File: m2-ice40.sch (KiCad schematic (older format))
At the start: 0 parts

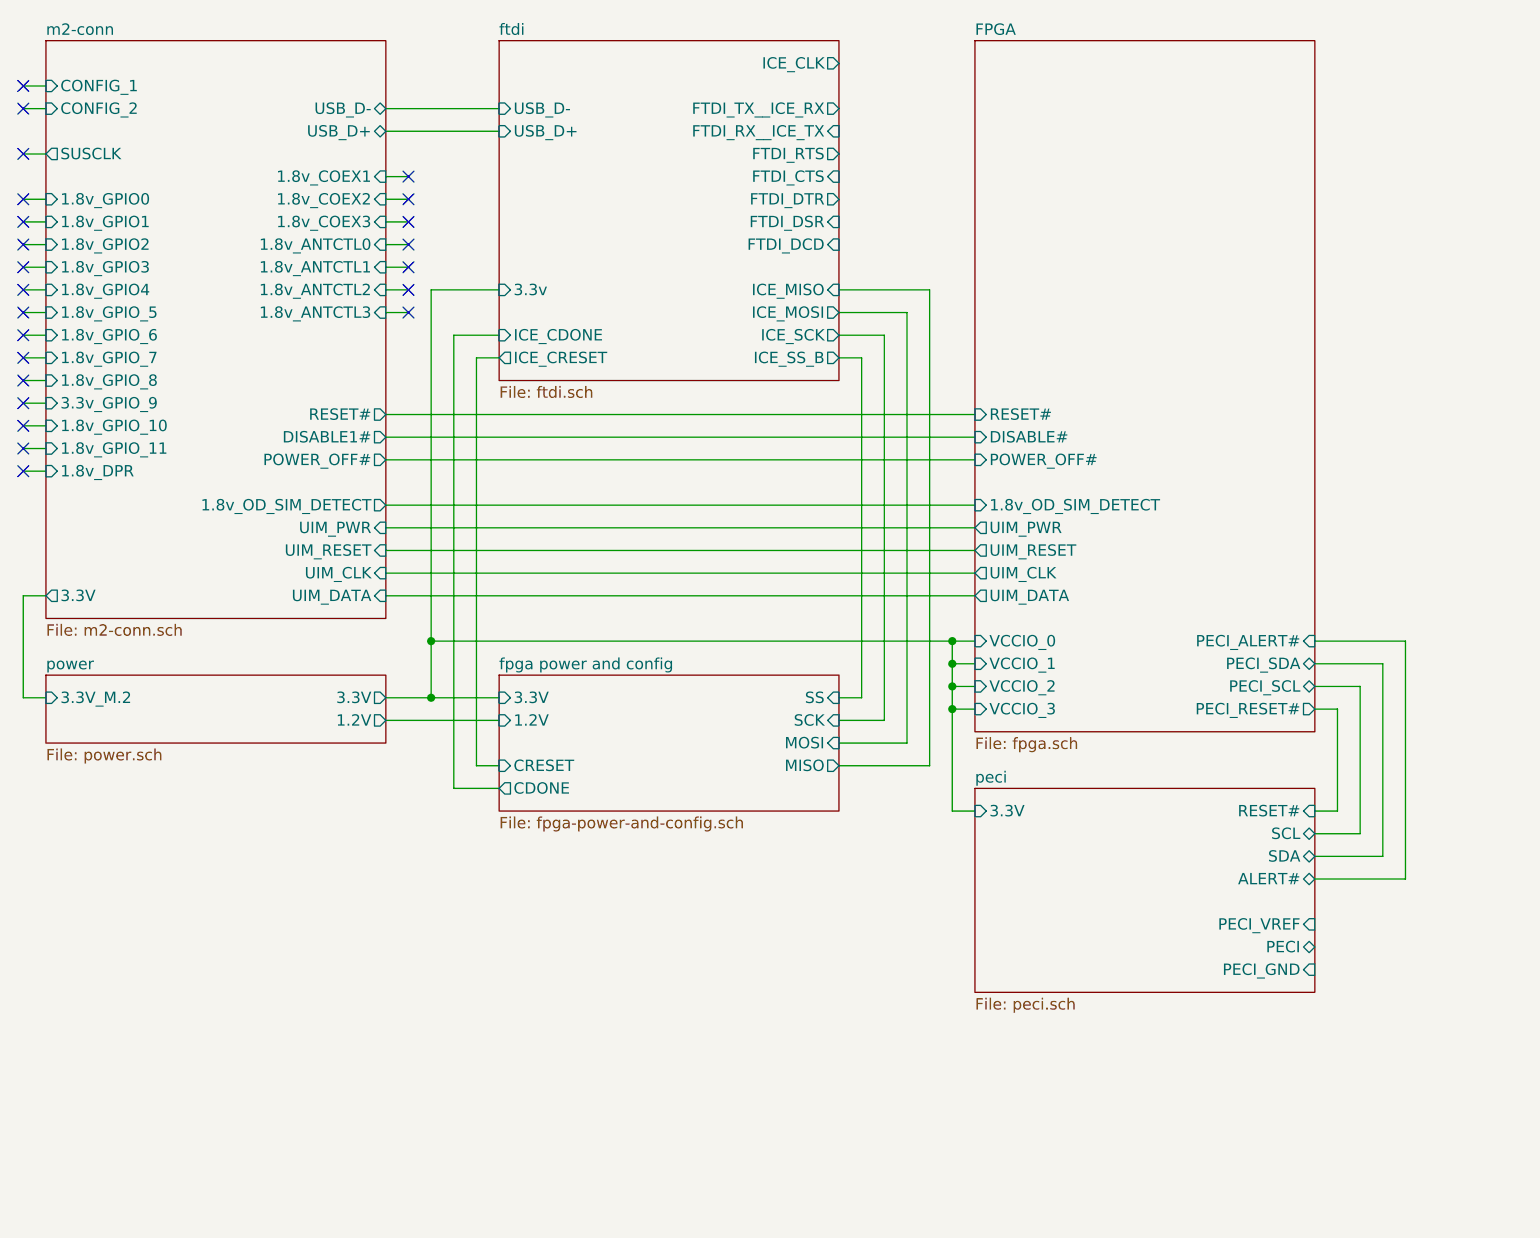
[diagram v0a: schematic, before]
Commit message: assigning pins, adding test points, placing stuff, etc
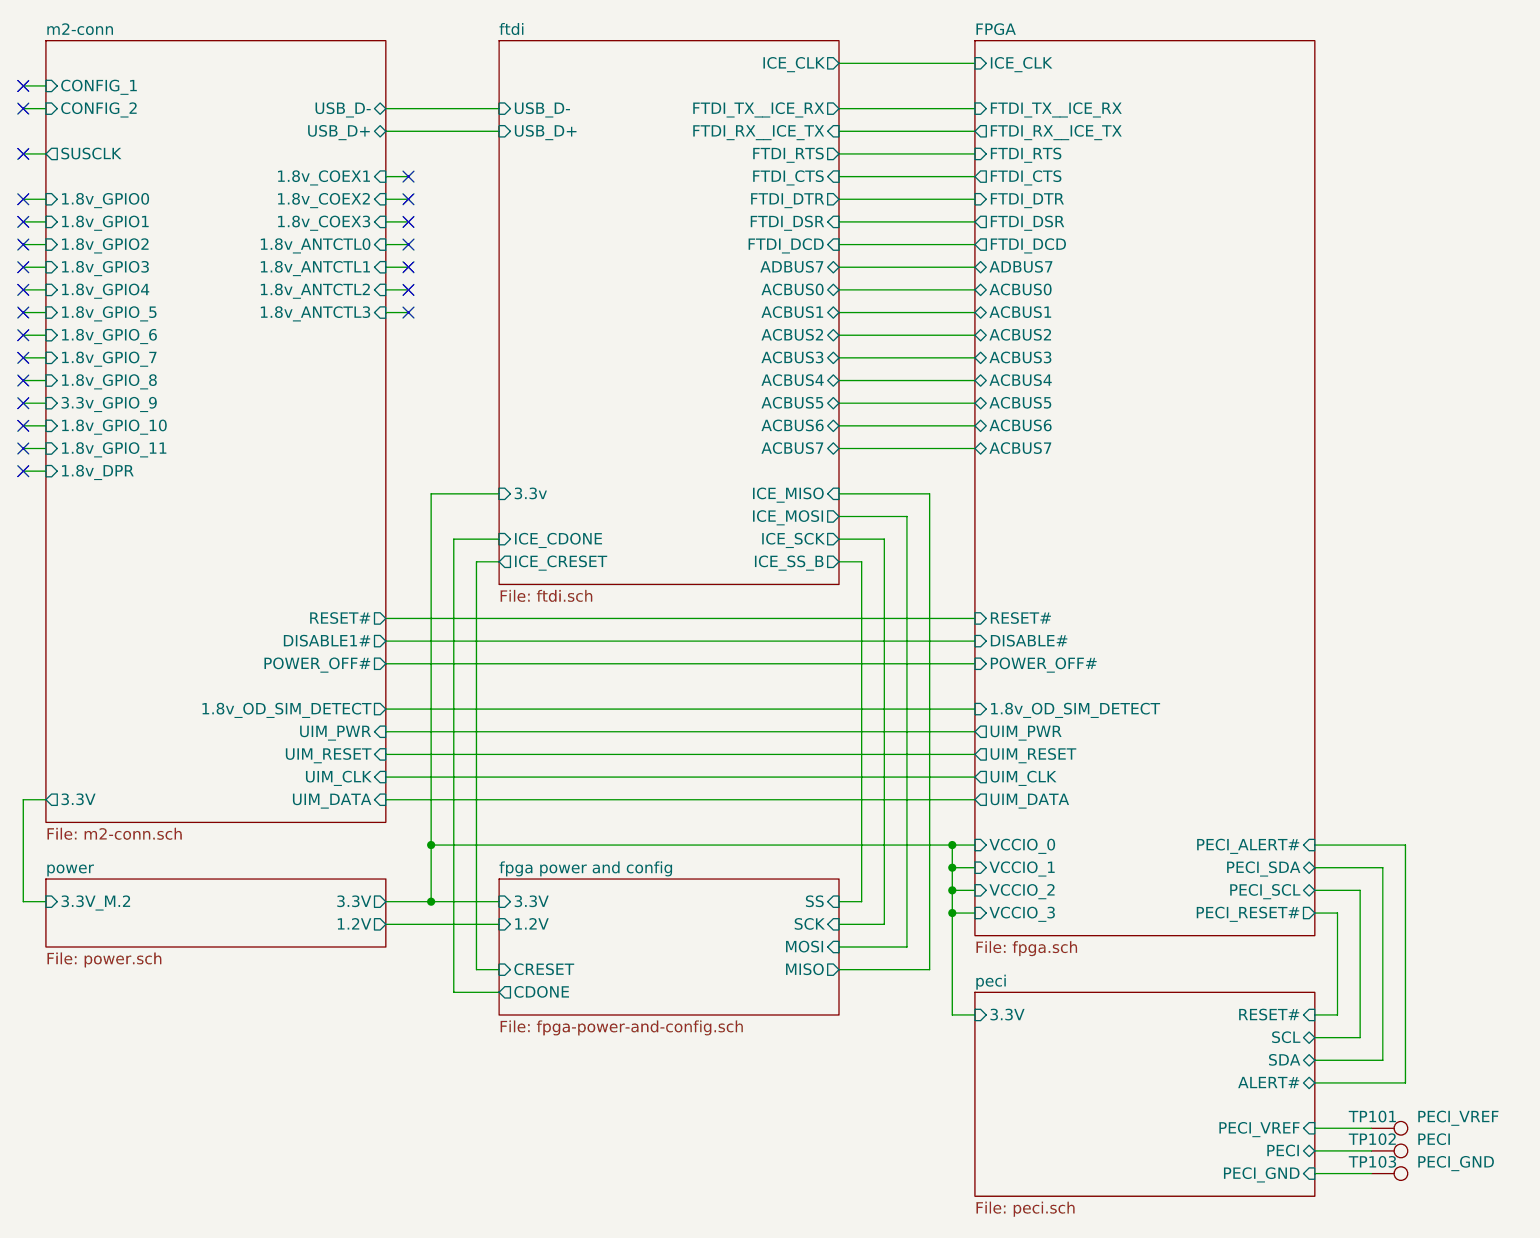
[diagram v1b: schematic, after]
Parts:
- added TP101: PECI_VREF, m2-ice40:TestPoint_Pad_0.5x1.5mm, symbol Connector:TestPoint
- added TP102: PECI, m2-ice40:TestPoint_Pad_0.5x1.5mm, symbol Connector:TestPoint
- added TP103: PECI_GND, m2-ice40:TestPoint_Pad_0.5x1.5mm, symbol Connector:TestPoint
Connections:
- net peci/PECI: now also TP102.1
- net peci/PECI_GND: now also TP103.1
- net peci/PECI_VREF: now also TP101.1
